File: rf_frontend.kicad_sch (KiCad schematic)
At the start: 16 parts, among them U301 BALFHB-WL-05D3, U302 BGS12SN6E6327XTSA1

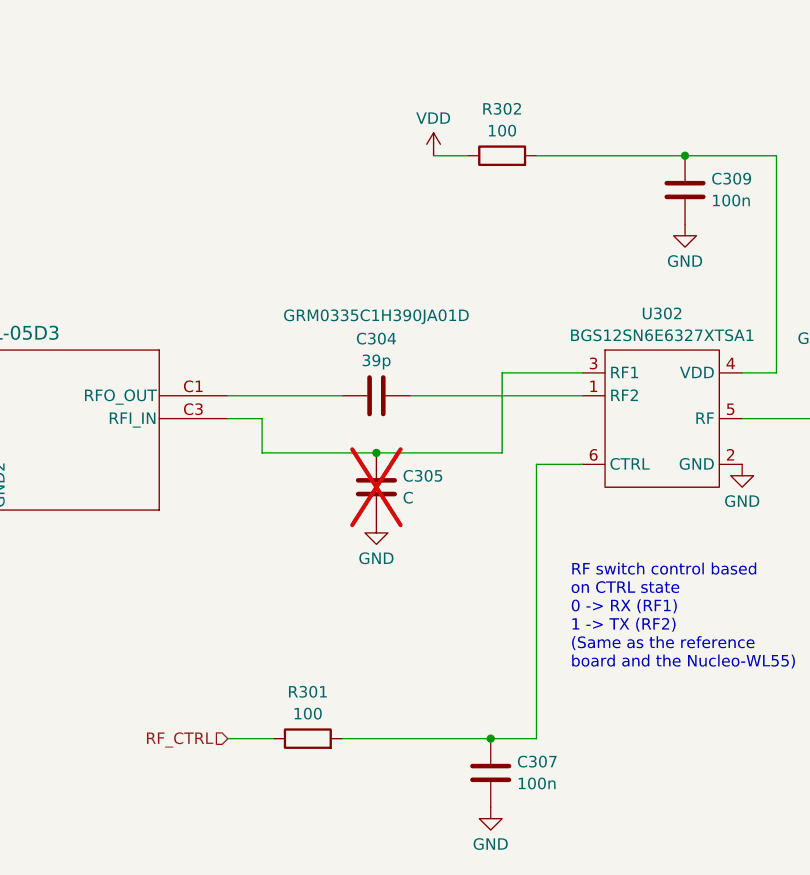
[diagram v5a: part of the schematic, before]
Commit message: groundplane settings tweak
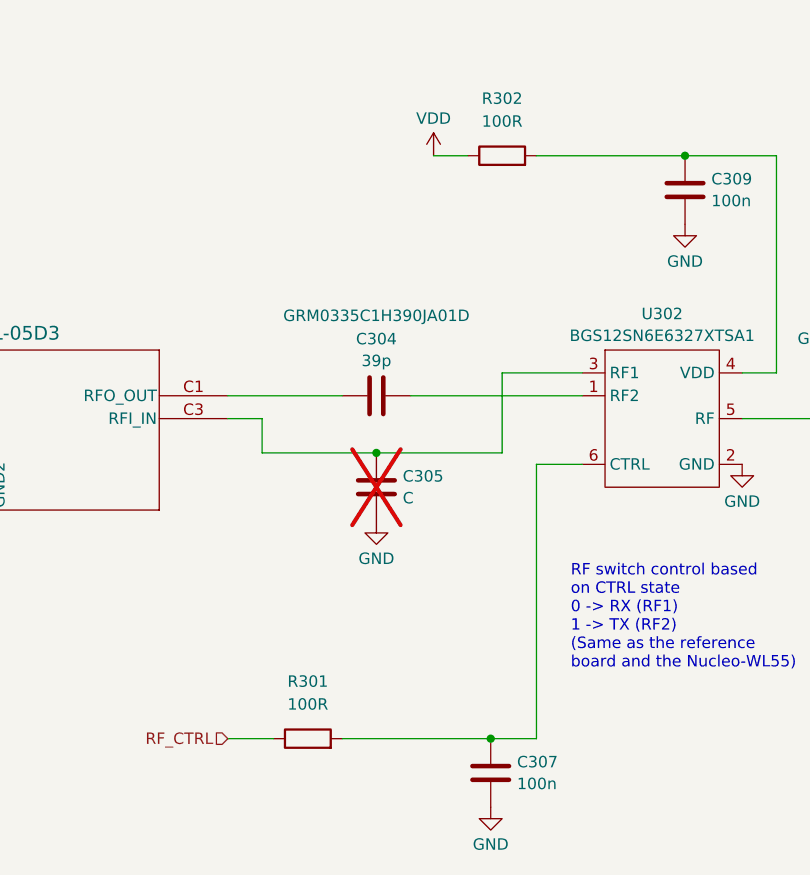
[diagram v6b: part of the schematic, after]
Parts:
- R301, R302: value 100 -> 100R
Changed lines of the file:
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@@
   (symbol (lib_id "Device:R") (at 167.64 72.39 90) (unit 1)
     (in_bom yes) (on_board yes) (dnp no) (fields_autoplaced)
-    (property "Reference" "R302" (at 167.64 67.2297 90)
-      (effects (font (size 1.27 1.27)))
-    )
-    (property "Value" "100" (at 167.64 69.6539 90)
+    (property "Reference" "R302" (at 167.64 66.04 90)
+      (effects (font (size 1.27 1.27)))
+    )
+    (property "Value" "100R" (at 167.64 68.58 90)
       (effects (font (size 1.27 1.27)))
     )
@@
   (symbol (lib_id "Device:R") (at 146.05 137.16 90) (unit 1)
     (in_bom yes) (on_board yes) (dnp no) (fields_autoplaced)
-    (property "Reference" "R301" (at 146.05 131.9997 90)
-      (effects (font (size 1.27 1.27)))
-    )
-    (property "Value" "100" (at 146.05 134.4239 90)
-      (effects (font (size 1.27 1.27)))
-    )
+    (property "Reference" "R301" (at 146.05 130.81 90)
+      (effects (font (size 1.27 1.27)))
+    )
+    (property "Value" "100R" (at 146.05 133.35 90)
+      (effects (font (size 1.27 1.27)))
+    )
